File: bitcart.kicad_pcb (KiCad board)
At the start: 4 copper layers, 160 x 90 mm, 136 parts, among them J1 Conn_01x03, J10 Hashboard3, J11 USB_OTG, J12 10018783-11200TLF, J13 690-008-221-904, J14 Conn_02x05_Odd_Even, J15 Conn_01x22_Female, J16 0455580003, J17 Molex 470531000, J2 Conn_02x07_Odd_Even, J3 Conn_01x03, J4 Hashboard0, J5 Hashboard1, J6 THD-02-R, J7 Micro_SD_Card_Det, J8 THD-20-R, J9 Hashboard2, Q1 DMP3013SFV-7, U10 PCA9546ARGVR, U11 EMC2301-1-ACZL-TR, U13 FSUSB42MUX, U14 74LVC1G07SE-7, U15 AP64501SP-13, U16 AP64501SP-13, U18 RT9742GGJ5, U3 MagJack-A70-112-331N126, U4 TPD4EUSB30, U5 74LVC1G07SE-7, U6 USB2514B-I/M2, U7 AP22653W6, U8 PCF85063AT/AAZ, U9 74LVC1G07SE-7, Y1 24MHz, Y2 X32K768S301

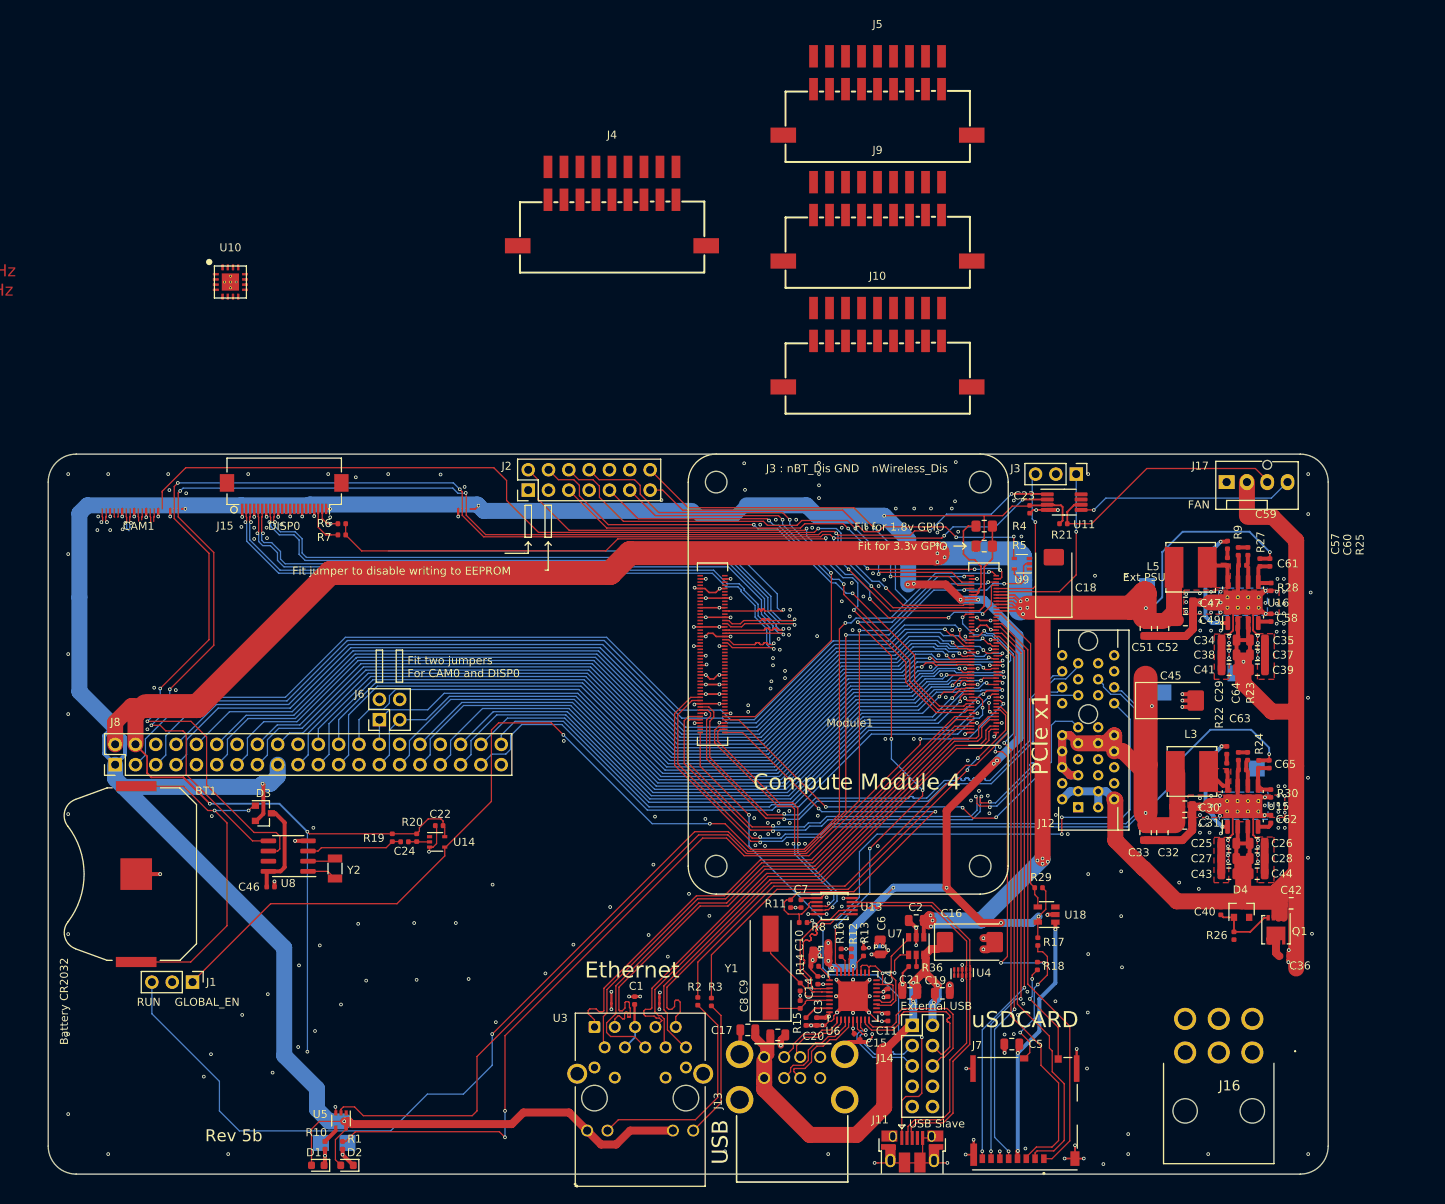
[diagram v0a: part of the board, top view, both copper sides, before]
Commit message: extended the board to make room for IO connectors. added the vertical display connector.
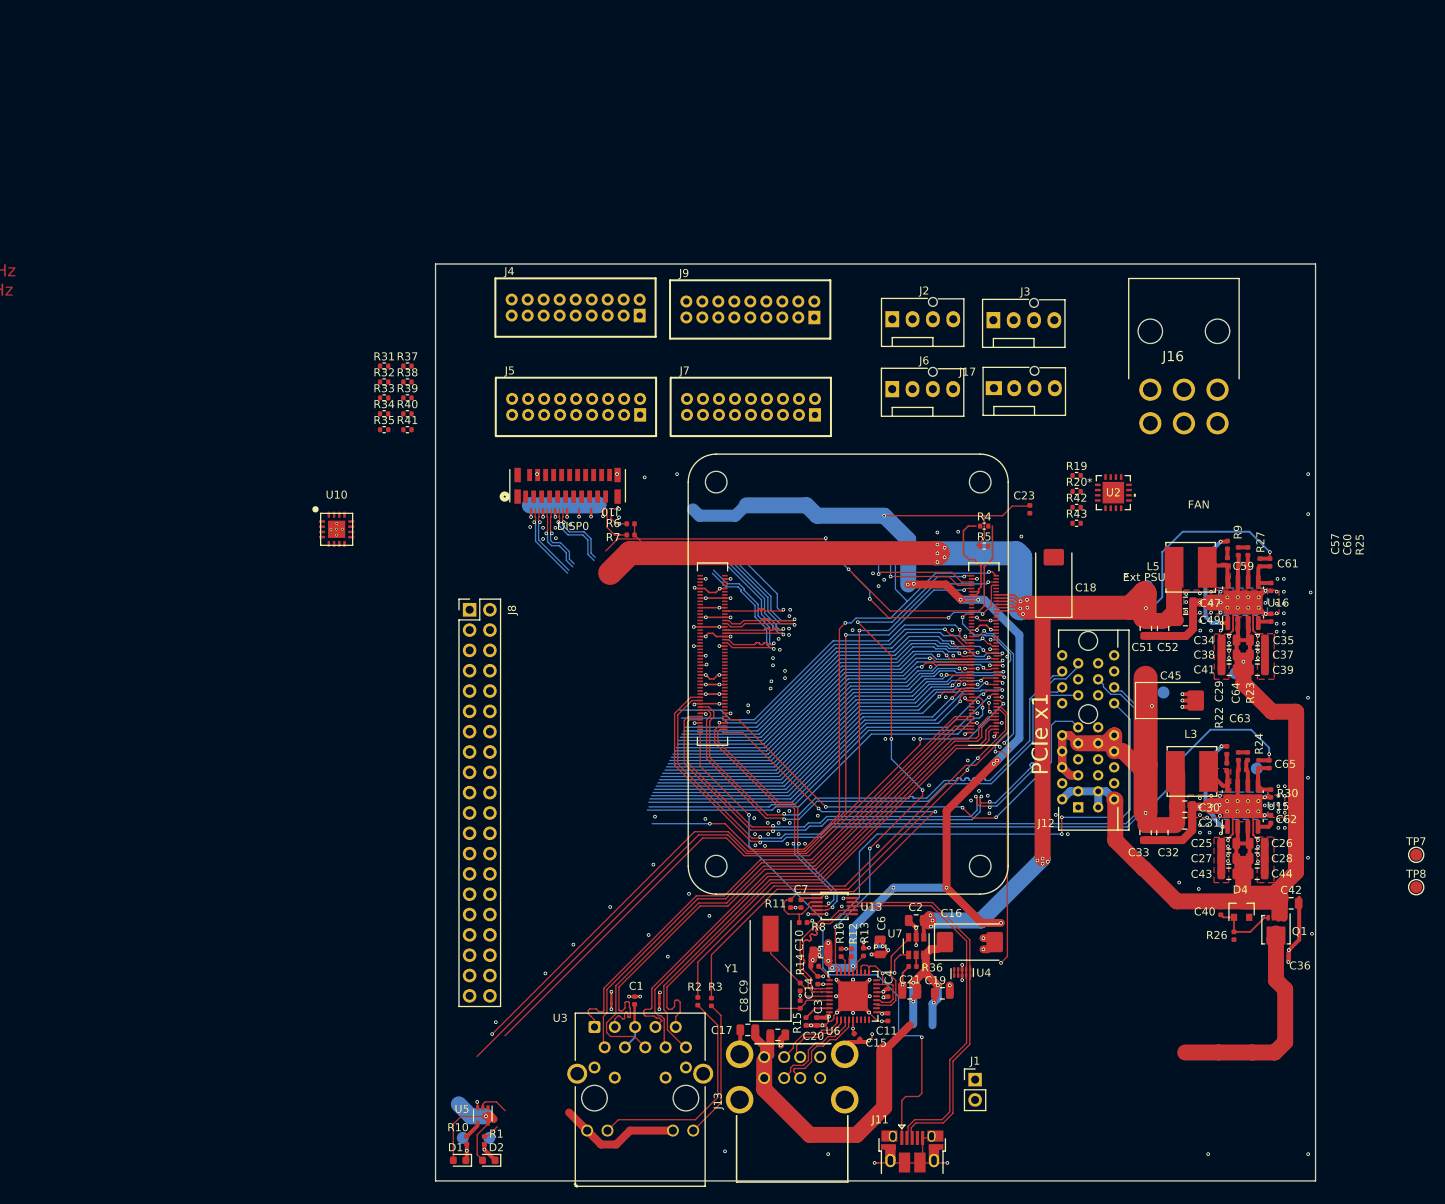
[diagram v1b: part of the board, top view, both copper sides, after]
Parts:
- removed BT1: Battery_Cell, Battery:BatteryHolder_Keystone_3034_1x20mm
- removed C22, C24, C46: 100n, Capacitor_SMD:C_0402_1005Metric
- removed C5: 10u, Capacitor_SMD:C_0805_2012Metric
- removed D3: BAT54C-7-F, Package_TO_SOT_SMD:SOT-23
- removed J14: Conn_02x05_Odd_Even, Connector_PinHeader_2.54mm:PinHeader_2x05_P2.54mm_Vertical
- removed J15: Conn_01x22_Female, CM4IO:Hirose_FH12-22S-0.5SH_1x22-1MP_P0.50mm_Horizontal
- removed R17, R18: nf, Resistor_SMD:R_0402_1005Metric
- removed R21: 36K 1%, Resistor_SMD:R_0402_1005Metric
- removed R29: 12K 1%, Resistor_SMD:R_0402_1005Metric
- removed U11: EMC2301-1-ACZL-TR, Package_SO:MSOP-8_3x3mm_P0.65mm
- removed U14, U9: 74LVC1G07SE-7, Package_TO_SOT_SMD:SOT-353_SC-70-5
- removed U18: RT9742GGJ5, Package_TO_SOT_SMD:SOT-23-5
- removed U8: PCF85063AT/AAZ, Package_SO:SOIC-8_3.9x4.9mm_P1.27mm
- removed Y2: X32K768S301, Crystal:Crystal_SMD_3215-2Pin_3.2x1.5mm
- added R31: 4.7K, Resistor_SMD:R_0402_1005Metric, F.Cu at (121.0, 59.0)
- added R32: 4.7K, Resistor_SMD:R_0402_1005Metric, F.Cu at (121.0, 61.0)
- added R33: 4.7K, Resistor_SMD:R_0402_1005Metric, F.Cu at (121.0, 63.0)
- added R34: 4.7K, Resistor_SMD:R_0402_1005Metric, F.Cu at (121.0, 65.0)
- added R35: 4.7K, Resistor_SMD:R_0402_1005Metric, F.Cu at (121.0, 67.0)
- added R37: 4.7K, Resistor_SMD:R_0402_1005Metric, F.Cu at (123.9, 59.0)
- added R38: 4.7K, Resistor_SMD:R_0402_1005Metric, F.Cu at (123.9, 61.0)
- added R39: 4.7K, Resistor_SMD:R_0402_1005Metric, F.Cu at (123.9, 63.0)
- added R40: 4.7K, Resistor_SMD:R_0402_1005Metric, F.Cu at (123.9, 65.0)
- added R41: 4.7K, Resistor_SMD:R_0402_1005Metric, F.Cu at (123.9, 67.0)
- added R42: 36K, Resistor_SMD:R_0402_1005Metric, F.Cu at (207.6, 76.7)
- added R43: 36K, Resistor_SMD:R_0402_1005Metric, F.Cu at (207.6, 78.6)
- added TP7: TestPoint, TestPoint:TestPoint_Pad_D1.5mm, F.Cu at (250.0, 120.1)
- added TP8: TestPoint, TestPoint:TestPoint_Pad_D1.5mm, F.Cu at (250.0, 124.1)
- added U2: EMC2305-1-AP-TR, bitcart:QFN16_4x4MC_MCH, F.Cu at (212.1, 74.8)
- J1: value Conn_01x03 -> Conn_01x02; footprint Connector_PinHeader_2.54mm:PinHeader_1x03_P2.54mm_Vertical -> Connector_PinHeader_2.54mm:PinHeader_1x02_P2.54mm_Vertical
- J10: value Hashboard3 -> Conn_01x22; footprint bitcart:CONN-SMD_X2026WRS-2X09D-LPSW -> bitcart:CON22_1X22_DUTB_HRS_HIR
- J2: value Conn_02x07_Odd_Even -> Molex 470531000; footprint Connector_PinHeader_2.54mm:PinHeader_2x07_P2.54mm_Vertical -> Connector:FanPinHeader_1x04_P2.54mm_Vertical
- J3: value Conn_01x03 -> Molex 470531000; footprint Connector_PinHeader_2.54mm:PinHeader_1x03_P2.54mm_Vertical -> Connector:FanPinHeader_1x04_P2.54mm_Vertical
- J4: footprint bitcart:CONN-SMD_X2026WRS-2X09D-LPSW -> bitcart:CONN-TH_X2026WV-2-09D-46SN
- J5: value Hashboard1 -> Hashboard2; footprint bitcart:CONN-SMD_X2026WRS-2X09D-LPSW -> bitcart:CONN-TH_X2026WV-2-09D-46SN
- J6: value THD-02-R -> Molex 470531000; footprint Connector_PinHeader_2.54mm:PinHeader_2x02_P2.54mm_Vertical -> Connector:FanPinHeader_1x04_P2.54mm_Vertical
- J7: value Micro_SD_Card_Det -> Hashboard1; footprint CM4IO:SDCARD_MOLEX_503398-1892 -> bitcart:CONN-TH_X2026WV-2-09D-46SN
- J9: value Hashboard2 -> Hashboard3; footprint bitcart:CONN-SMD_X2026WRS-2X09D-LPSW -> bitcart:CONN-TH_X2026WV-2-09D-46SN
- R19, R20: value 510K 1% -> 36K
- R4: value nf -> 4.7K; footprint Resistor_SMD:R_0805_2012Metric_Pad1.15x1.40mm_HandSolder -> Resistor_SMD:R_0402_1005Metric
- R5: value 0R -> 4.7K; footprint Resistor_SMD:R_0805_2012Metric_Pad1.15x1.40mm_HandSolder -> Resistor_SMD:R_0402_1005Metric
- TP1, TP2, TP3, TP4, TP5, TP6: footprint TestPoint:TestPoint_Pad_2.0x2.0mm -> TestPoint:TestPoint_Pad_D1.5mm
- moved J1 98.6 mm to (194.9, 148.2), turned to 0 degrees
- moved R19 96.8 mm to (207.6, 72.7), turned to 0 degrees
- moved J7 94.8 mm to (166.8, 64.1), turned to 0 degrees
- moved R20 93.2 mm to (207.6, 74.7), turned to 0 degrees
- moved J16 83.8 mm to (216.8, 61.9), turned to 0 degrees
- moved J6 76.3 mm to (184.5, 61.9), turned to 0 degrees
- moved J5 54.2 mm to (145.0, 64.1)
- moved J2 50.3 mm to (184.5, 53.1), turned to 0 degrees
- moved J8 48.4 mm to (131.7, 89.5), turned to 0 degrees
- moved J10 42.4 mm to (143.9, 74.0), turned to 180 degrees
- moved R6 36.1 mm to (151.8, 78.7)
- moved R7 36.1 mm to (151.8, 80.1)
- moved U10 33.6 mm to (115.1, 79.4)
- moved J17 31.4 mm to (197.2, 61.8)
- moved J3 21.9 mm to (197.1, 53.3), turned to 0 degrees
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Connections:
- J1 pad 1: /CM4_GPIO ( Ethernet, GPIO, SDCARD)/GLOBAL_EN -> GND
- J1 pad 2: GND -> /CM4_GPIO ( Ethernet, GPIO, SDCARD)/nRPIBOOT
- J10 pad 11: /hashboards/TXD3 -> unconnected-(J10-Pin_11-Pad11)
- J10 pad 12: /hashboards/RXD3 -> unconnected-(J10-Pin_12-Pad12)
- J10 pad 14: GND -> unconnected-(J10-Pin_14-Pad14)
- J10 pad 15: /hashboards/RST3 -> unconnected-(J10-Pin_15-Pad15)
- J10 pad 16: /hashboards/3V3 -> GND
- J10 pad 19: (no net) -> GND
- J10 pad 2: GND -> /CM4_HighSpeed/DSI0_D0_N
- J10 pad 20: (no net) -> /CM4_GPIO ( Ethernet, GPIO, SDCARD)/ID_SC
- J10 pad 3: /hashboards/SDA3 -> /CM4_HighSpeed/DSI0_D0_P
- J10 pad 4: /hashboards/SCL3 -> GND
- J10 pad 5: /hashboards/PLUG3 -> /CM4_HighSpeed/DSI0_D1_N
- J10 pad 6: /hashboards/A2-3 -> /CM4_HighSpeed/DSI0_D1_P
- J10 pad 7: /hashboards/A1-3 -> GND
- J10 pad 8: /hashboards/A0-3 -> /CM4_HighSpeed/DSI0_C_N
- J10 pad 9: GND -> /CM4_HighSpeed/DSI0_C_P
- J2 pad 2: /CM4_GPIO ( Ethernet, GPIO, SDCARD)/nRPIBOOT -> /+12v
- J2 pad 3: GND -> Net-(J2-Pin_3)
- J2 pad 4: /CM4_GPIO ( Ethernet, GPIO, SDCARD)/EEPROM_nWP -> Net-(J2-Pin_4)
- J3 pad 1: /CM4_GPIO ( Ethernet, GPIO, SDCARD)/WL_nDis -> GND
- J3 pad 2: GND -> /+12v
- J3 pad 3: /CM4_GPIO ( Ethernet, GPIO, SDCARD)/BT_nDis -> Net-(J3-Pin_3)
- J5 pad 11: /hashboards/TXD1 -> /hashboards/TXD2
- J5 pad 12: /hashboards/RXD1 -> /hashboards/RXD2
- J5 pad 15: /hashboards/RST1 -> /hashboards/RST2
- J5 pad 3: /hashboards/SDA1 -> /hashboards/SDA2
- J5 pad 4: /hashboards/SCL1 -> /hashboards/SCL2
- J5 pad 5: /hashboards/PLUG1 -> /hashboards/PLUG2
- J5 pad 6: /hashboards/A2-1 -> /hashboards/A2-2
- J5 pad 7: /hashboards/A1-1 -> /hashboards/A1-2
- J5 pad 8: /hashboards/A0-1 -> /hashboards/A0-2
- J6 pad 1: /CM4_GPIO ( Ethernet, GPIO, SDCARD)/ID_SC -> GND
- J6 pad 2: /CM4_HighSpeed/SCL1 -> /+12v
- J6 pad 3: /CM4_GPIO ( Ethernet, GPIO, SDCARD)/ID_SD -> Net-(J6-Pin_3)
- J6 pad 4: /CM4_HighSpeed/SDA1 -> Net-(J6-Pin_4)
- J7 pad 1: /CM4_GPIO ( Ethernet, GPIO, SDCARD)/SD_DAT2 -> GND
- J7 pad 10: Net-(J7-DET_A) -> GND
- J7 pad 11: GND -> /hashboards/TXD1
- J7 pad 2: /CM4_GPIO ( Ethernet, GPIO, SDCARD)/SD_DAT3 -> GND
- J7 pad 3: /CM4_GPIO ( Ethernet, GPIO, SDCARD)/SD_CMD -> /hashboards/SDA1
- J7 pad 4: /CM4_GPIO ( Ethernet, GPIO, SDCARD)/SD_PWR -> /hashboards/SCL1
- J7 pad 5: /CM4_GPIO ( Ethernet, GPIO, SDCARD)/SD_CLK -> /hashboards/PLUG1
- J7 pad 6: GND -> /hashboards/A2-1
- J7 pad 7: /CM4_GPIO ( Ethernet, GPIO, SDCARD)/SD_DAT0 -> /hashboards/A1-1
- J7 pad 8: /CM4_GPIO ( Ethernet, GPIO, SDCARD)/SD_DAT1 -> /hashboards/A0-1
- J7 pad 9: Net-(J7-DET_B) -> GND
- J9 pad 11: /hashboards/TXD2 -> /hashboards/TXD3
- J9 pad 12: /hashboards/RXD2 -> /hashboards/RXD3
- J9 pad 15: /hashboards/RST2 -> /hashboards/RST3
- J9 pad 3: /hashboards/SDA2 -> /hashboards/SDA3
- J9 pad 4: /hashboards/SCL2 -> /hashboards/SCL3
- J9 pad 5: /hashboards/PLUG2 -> /hashboards/PLUG3
- J9 pad 6: /hashboards/A2-2 -> /hashboards/A2-3
- J9 pad 7: /hashboards/A1-2 -> /hashboards/A1-3
- J9 pad 8: /hashboards/A0-2 -> /hashboards/A0-3
- Module1 pad 78: /CM4_GPIO ( Ethernet, GPIO, SDCARD)/GPIO_VREF -> /+3.3v
- Module1 pad 80: /RTC , Wakeup, FAN/SCL -> /Fan/SCL
- Module1 pad 82: /RTC , Wakeup, FAN/SDA -> /Fan/SDA
- Module1 pad 97: /CM4_GPIO ( Ethernet, GPIO, SDCARD)/CAM_GPIO -> unconnected-(Module1A-Camera_GPIO-Pad97)
- R19 pad 1: /RTC , Wakeup, FAN/nRTC_INT -> /+3.3v
- R19 pad 2: /+5v -> Net-(J6-Pin_3)
- R20 pad 1: Net-(C24-Pad1) -> /+3.3v
- R20 pad 2: /+5v -> Net-(J3-Pin_3)
- R4 pad 1: /CM4_GPIO ( Ethernet, GPIO, SDCARD)/+1.8v -> GND
- R4 pad 2: /CM4_GPIO ( Ethernet, GPIO, SDCARD)/GPIO_VREF -> /hashboards/A1-0
- R5 pad 1: /+3.3v -> /hashboards/A0-0
- R5 pad 2: /CM4_GPIO ( Ethernet, GPIO, SDCARD)/GPIO_VREF -> GND
- R6 pad 1: /CM4_GPIO ( Ethernet, GPIO, SDCARD)/GPIO_VREF -> /+3.3v
- R6 pad 2: /CM4_HighSpeed/SDA1 -> /CM4_GPIO ( Ethernet, GPIO, SDCARD)/ID_SD
- R7 pad 1: /CM4_GPIO ( Ethernet, GPIO, SDCARD)/GPIO_VREF -> /+3.3v
- R7 pad 2: /CM4_HighSpeed/SCL1 -> /CM4_GPIO ( Ethernet, GPIO, SDCARD)/ID_SC
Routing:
- net /RTC , Wakeup, FAN/SCL: track 201.2 -> 0.00 mm, vias 8 -> 0
- net /RTC , Wakeup, FAN/SDA: track 194.6 -> 0.00 mm, vias 8 -> 0
- net /+3.3v: track 458.4 -> 288.6 mm, vias 27 -> 24
- net /+5v: track 350.6 -> 196.6 mm, vias 23 -> 19
- net /CM4_GPIO ( Ethernet, GPIO, SDCARD)/CAM_GPIO: track 117.8 -> 0.00 mm, vias 4 -> 0
- net /CM4_GPIO ( Ethernet, GPIO, SDCARD)/GLOBAL_EN: track 196.2 -> 79.6 mm, vias 5 -> 3
- net /CM4_GPIO ( Ethernet, GPIO, SDCARD)/GPIO_VREF: track 97.8 -> 0.00 mm, vias 2 -> 0
- net /CM4_GPIO ( Ethernet, GPIO, SDCARD)/GPIO2: track 122.9 -> 43.4 mm
- net /CM4_GPIO ( Ethernet, GPIO, SDCARD)/GPIO3: track 119.8 -> 42.2 mm
- net /CM4_GPIO ( Ethernet, GPIO, SDCARD)/GPIO4: track 116.5 -> 41.6 mm
- net /CM4_GPIO ( Ethernet, GPIO, SDCARD)/GPIO14: track 117.8 -> 44.7 mm
- net /CM4_GPIO ( Ethernet, GPIO, SDCARD)/SD_DAT2: track 73.0 -> 0.00 mm
- net /CM4_GPIO ( Ethernet, GPIO, SDCARD)/RUN_PG: track 170.6 -> 97.6 mm, vias 4 -> 3
- net /CM4_GPIO ( Ethernet, GPIO, SDCARD)/SD_DAT3: track 71.8 -> 0.00 mm
- net /CM4_GPIO ( Ethernet, GPIO, SDCARD)/SD_DAT1: track 70.4 -> 0.00 mm, vias 2 -> 0
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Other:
- board size 160 x 90 mm -> 110 x 114.6 mm
- board text removed: "Battery CR2032"
- board text removed: "CAM1"
- board text removed: "Compute Module 4"
- board text removed: "Ethernet"
- board text removed: "External USB"
- board text removed: "Fit for 1.8v GPIO"
- board text removed: "Fit for 3.3v GPIO"
- board text removed: "Fit jumper to disable writing to EEPROM"
- board text removed: "Fit two jumpers For CAM0 and DISP0"
- board text removed: "J3 : nBT_Dis GND"
- board text removed: "RUN GLOBAL_EN"
- board text removed: "Rev 5b"
- board text removed: "USB"
- board text removed: "USB Slave"
- board text removed: "nWireless_Dis"
- board text removed: "uSDCARD"

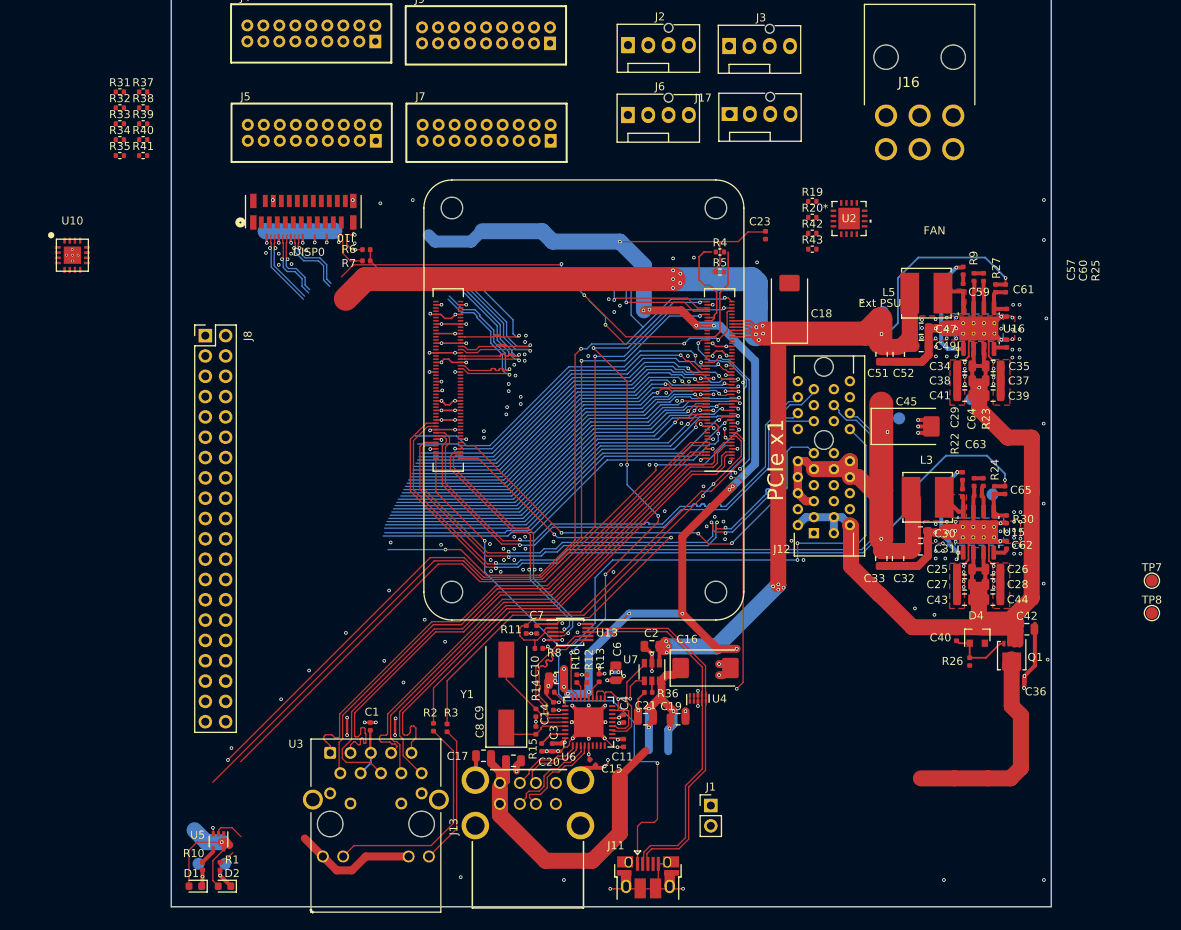
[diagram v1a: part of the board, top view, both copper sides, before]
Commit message: added the PSU control connector.
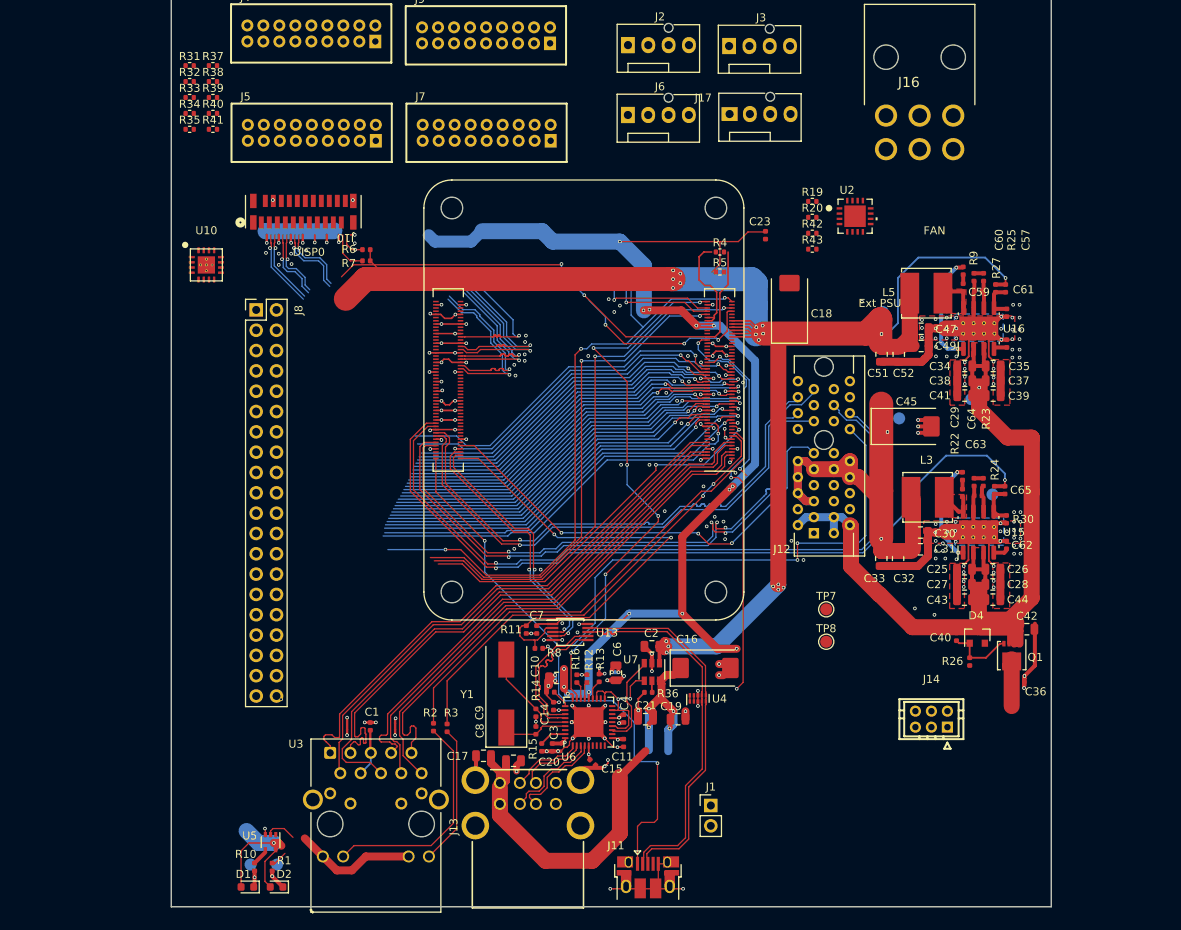
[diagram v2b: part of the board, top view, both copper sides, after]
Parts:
- added J14: Conn_02x03_Odd_Even, bitcart:CONN-TH_6P-P2.00_PHD-2X3A, F.Cu at (222.4, 137.4)
- moved TP7 40.9 mm to (209.3, 123.7)
- moved TP8 40.9 mm to (209.3, 127.7)
- moved U10 16.8 mm to (131.8, 80.6)
- moved R35 9.32 mm to (129.7, 63.7)
- moved R31 9.32 mm to (129.7, 55.7)
- moved R32 9.32 mm to (129.7, 57.7)
- moved R33 9.32 mm to (129.7, 59.7)
- moved R34 9.32 mm to (129.7, 61.7)
- moved R41 9.32 mm to (132.6, 63.7)
- moved R37 9.32 mm to (132.6, 55.7)
- moved R38 9.32 mm to (132.6, 57.7)
- moved R39 9.32 mm to (132.6, 59.7)
- moved R40 9.32 mm to (132.6, 61.7)
- moved J8 7.12 mm to (138.0, 86.2)
- moved D1 6.51 mm to (136.9, 158.4)
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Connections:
- J4 pad 11: /hashboards/TXD0 -> /CM4_GPIO ( Ethernet, GPIO, SDCARD)/GPIO14
- J4 pad 12: /hashboards/RXD0 -> /CM4_GPIO ( Ethernet, GPIO, SDCARD)/GPIO15
- J4 pad 15: /hashboards/RST0 -> /CM4_GPIO ( Ethernet, GPIO, SDCARD)/GPIO17
- J4 pad 5: /hashboards/PLUG0 -> /CM4_GPIO ( Ethernet, GPIO, SDCARD)/GPIO16
- J5 pad 11: /hashboards/TXD2 -> /CM4_GPIO ( Ethernet, GPIO, SDCARD)/GPIO8
- J5 pad 12: /hashboards/RXD2 -> /CM4_GPIO ( Ethernet, GPIO, SDCARD)/GPIO12
- J5 pad 15: /hashboards/RST2 -> /CM4_GPIO ( Ethernet, GPIO, SDCARD)/GPIO11
- J5 pad 5: /hashboards/PLUG2 -> /CM4_GPIO ( Ethernet, GPIO, SDCARD)/GPIO10
- J7 pad 11: /hashboards/TXD1 -> /CM4_GPIO ( Ethernet, GPIO, SDCARD)/GPIO4
- J7 pad 12: /hashboards/RXD1 -> /CM4_GPIO ( Ethernet, GPIO, SDCARD)/GPIO5
- J7 pad 15: /hashboards/RST1 -> /CM4_GPIO ( Ethernet, GPIO, SDCARD)/GPIO7
- J7 pad 5: /hashboards/PLUG1 -> /CM4_GPIO ( Ethernet, GPIO, SDCARD)/GPIO6
- J9 pad 11: /hashboards/TXD3 -> /CM4_GPIO ( Ethernet, GPIO, SDCARD)/GPIO13
- J9 pad 12: /hashboards/RXD3 -> /CM4_GPIO ( Ethernet, GPIO, SDCARD)/GPIO9
- J9 pad 15: /hashboards/RST3 -> /CM4_GPIO ( Ethernet, GPIO, SDCARD)/GPIO18
- J9 pad 5: /hashboards/PLUG3 -> /CM4_GPIO ( Ethernet, GPIO, SDCARD)/GPIO19
- Module1 pad 80: /Fan/SCL -> /SCL
- Module1 pad 82: /Fan/SDA -> /SDA
- U10 pad 12: /hashboards/SCL -> /SCL
- U10 pad 13: /hashboards/SDA -> /SDA
- U2 pad 1: /Fan/SDA -> /SDA
- U2 pad 2: /Fan/SCL -> /SCL
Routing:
- net /CM4_GPIO ( Ethernet, GPIO, SDCARD)/nPWR_LED: track 107.7 -> 68.5 mm
- net /CM4_GPIO ( Ethernet, GPIO, SDCARD)/RUN_PG: track 97.6 -> 61.8 mm, vias 3 -> 2
- net Net-(Module1A-PI_nLED_Activity): track 84.9 -> 50.0 mm
- net Net-(Q1-D): track 31.4 -> 10.1 mm
- net GND: vias 283 -> 235
- net /CM4_GPIO ( Ethernet, GPIO, SDCARD)/GPIO21: vias 1 -> 2
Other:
- board text removed: "PCIe x1"
